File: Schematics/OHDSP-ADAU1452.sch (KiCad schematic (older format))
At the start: 0 parts

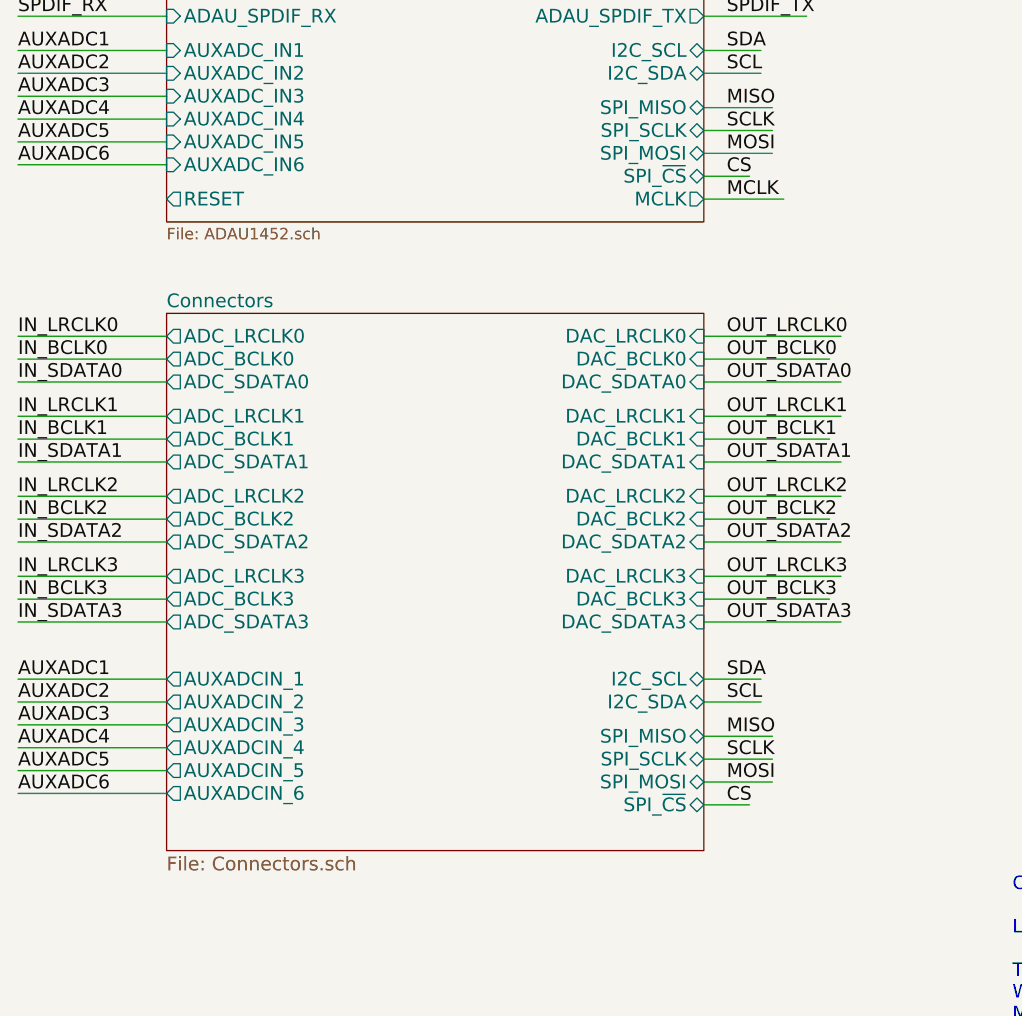
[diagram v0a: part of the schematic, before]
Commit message: PCB work, added manual reset to Pi header
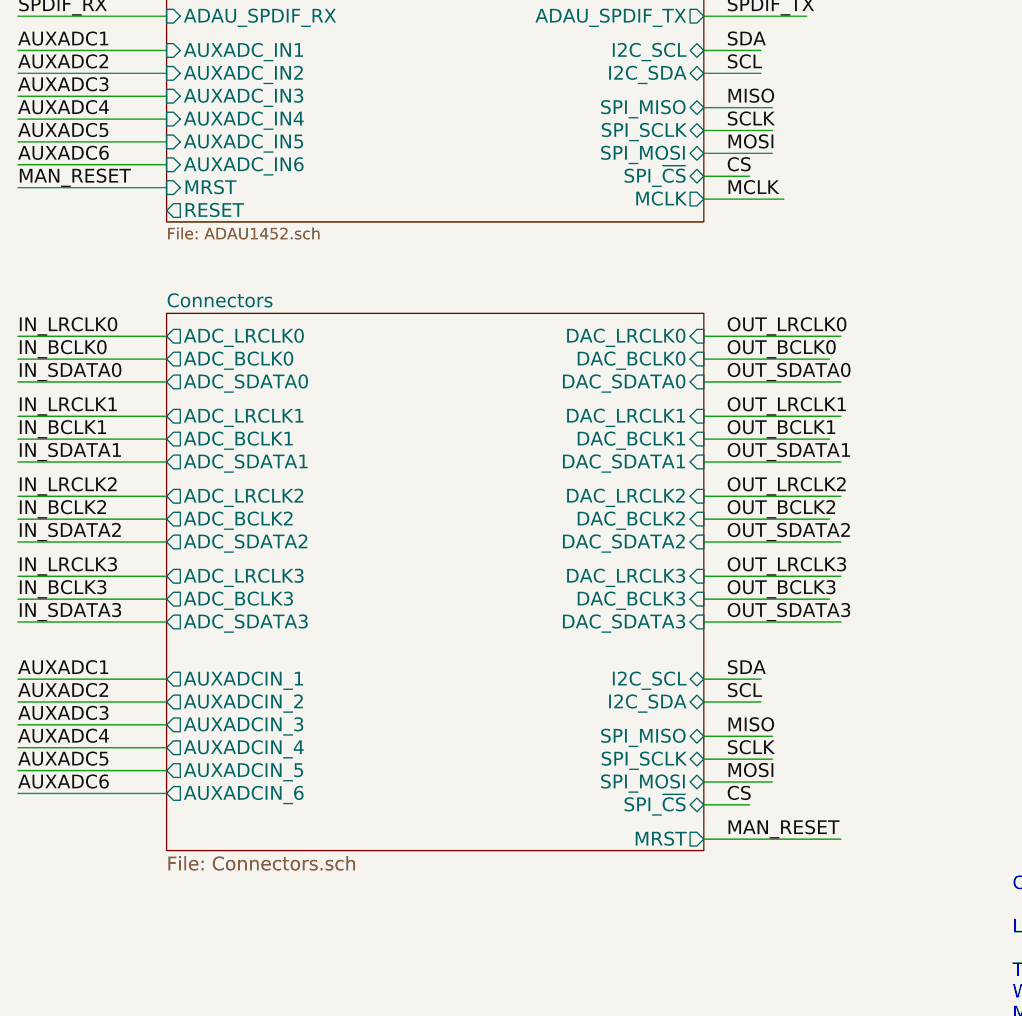
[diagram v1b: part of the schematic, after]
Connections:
- net labels added: MAN_RESET
- wire segments 78 -> 80
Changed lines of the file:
@@
 F39 "SPI_~CS" B R 5650 3300 60
 F40 "MCLK" O R 5650 3400 60
-F41 "RESET" O L 3300 3400 60
+F41 "RESET" O L 3300 3450 60
+F42 "MRST" I L 3300 3350 60
 $EndSheet
 $Sheet
@@
 F36 "DAC_BCLK3" I R 5650 5150 60
 F37 "DAC_SDATA3" I R 5650 5250 60
+F38 "MRST" O R 5650 6200 60
 $EndSheet
 Text Label 2650 4000 0    60   ~ 0
@@
 Text Notes 7000 7100 0    59   ~ 0
 Copyright Paul Janicki 2015\n\nLicensed under the TAPR Open Hardware License (www.tapr.org/OHL).\n\nThis documentation is distributed\nWITHOUT ANY EXPRESS OR IMPLIED WARRANTY, INCLUDING OF\nMERCHANTABILITY, SATISFACTORY QUALITY AND FITNESS FOR A\nPARTICULAR PURPOSE.\n
+Text Label 5750 6200 0    60   ~ 0
+MAN_RESET
+Wire Wire Line
+	5650 6200 6250 6200
+Text Label 2650 3350 0    60   ~ 0
+MAN_RESET
+Wire Wire Line
+	2650 3350 3300 3350
 $EndSCHEMATC
